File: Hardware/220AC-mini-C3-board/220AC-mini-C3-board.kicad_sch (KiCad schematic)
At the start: 21 parts, among them J1 AC MAINS POWER, J2 ON/OFF switch, J4 Conn_01x06_Pin, K1 HF163-F, Q1 Q_NPN_CBE, Q2 Q_NPN_CBE

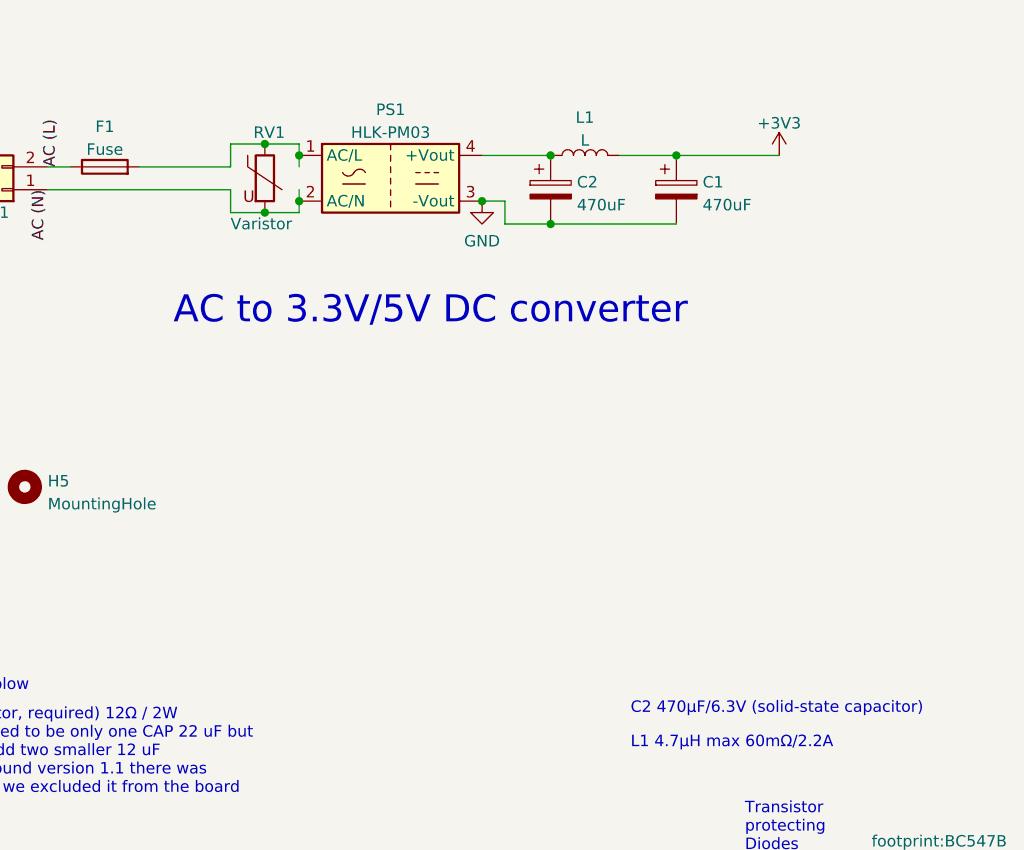
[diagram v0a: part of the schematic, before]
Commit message: Added Power Sensor connector
Addded Power Sensor ASML115
finished for production
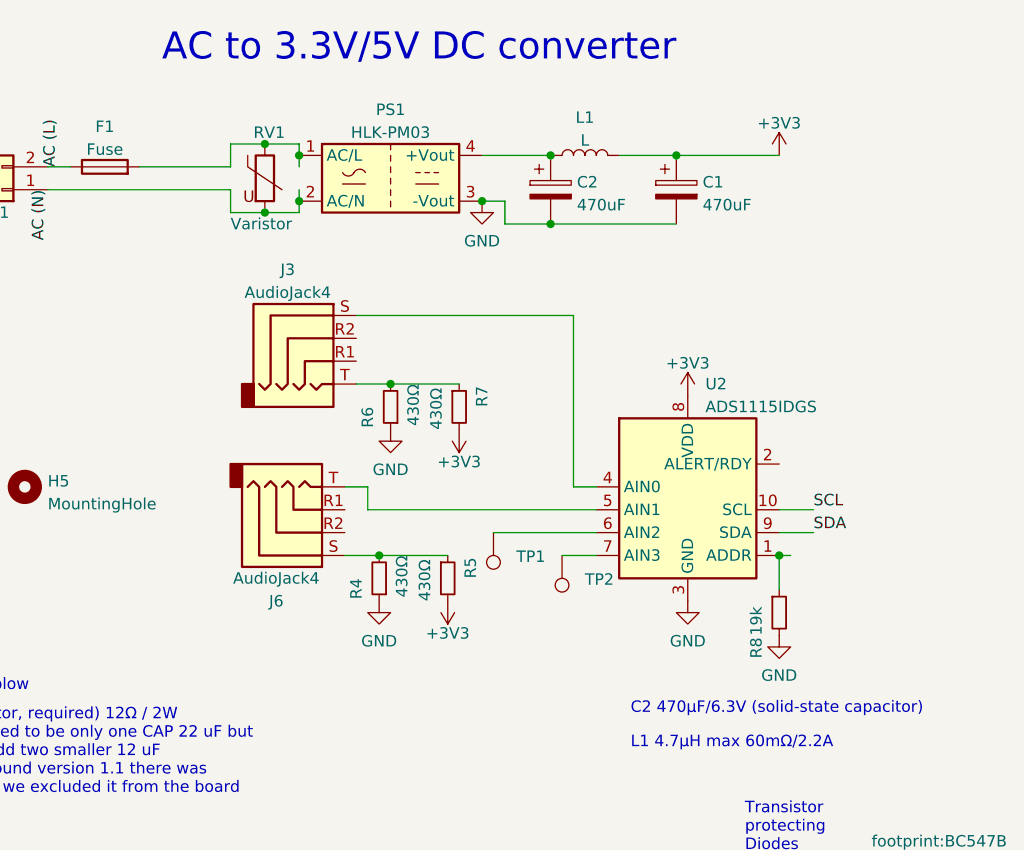
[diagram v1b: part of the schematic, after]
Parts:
- added J3, J6: AudioJack4, Connector_Audio:Jack_3.5mm_PJ320D_Horizontal, symbol Connector_Audio:AudioJack4
- added R4, R5, R6, R7: 430Ω, Resistor_SMD:R_0805_2012Metric_Pad1.20x1.40mm_HandSolder, symbol Device:R_Small
- added R8: 19k, Resistor_SMD:R_0603_1608Metric, symbol Device:R_Small
- added TP1, TP2: TestPoint, TestPoint:TestPoint_Pad_D1.5mm, symbol Connector:TestPoint
- added U2: ADS1115IDGS, Package_SO:TSSOP-10_3x3mm_P0.5mm, symbol Analog_ADC:ADS1115IDGS
- R2, R3: footprint Resistor_SMD:R_0603_1608Metric -> Resistor_SMD:R_0805_2012Metric_Pad1.20x1.40mm_HandSolder
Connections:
- net +3V3: now also R5.2, R7.2, U2.8 (VDD)
- net GND: now also R4.1, R6.1, R8.2, U2.3 (GND)
- net SCL: now also U2.10 (SCL)
- net SDA: now also U2.9 (SDA)
- new net: J6.S, R4.2, R5.1
- new net: R8.1, U2.1 (ADDR)
- new net: J3.T, R6.2, R7.1
- new net: TP2.1, U2.7 (AIN3)
- new net: J3.S, U2.4 (AIN0)
- new net: J6.T, U2.5 (AIN1)
- new net: TP1.1, U2.6 (AIN2)
